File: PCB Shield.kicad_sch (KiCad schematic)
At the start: 49 parts, among them J1 Conn_01x20, J10 Conn_01x04_Socket, J11 Conn_01x04_Socket, J12 TB002-500-02BE, J13 TB002-500-02BE, J14 TB002-500-02BE, J15 TB002-500-02BE, J16 TB002-500-02BE, J17 TB002-500-02BE, J18 TB002-500-02BE, J19 TB002-500-02BE, J2 Conn_01x20, J3 Conn_01x20, J4 Conn_01x20, J5 TB002-500-02BE, J6 Conn_01x08_Socket, J9 Conn_01x04_Socket, Q1 NMOS, U1 74AHCT125S14-13

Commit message: 5:30am progress so far
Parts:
- removed C10, C5, C6, C7, C8, C9: 470uF, Capacitor_SMD:C_1206_3216Metric, symbol Device:C
- removed D1, D2, D3, D4, D5, D6, D7, D8: CMD17-21VGD/TR8, 1A PCB 196:LED0805N_CML, symbol 1A 196 schematics:LED_CMD17-21VGD_TR8
- removed J12, J13, J14, J15, J16, J17, J5: TB002-500-02BE, 1A PCB 196:Conn CUI_TB002-500-02BE, symbol 1A 196 schematics:TB002-500-02BE
- removed R1, R2, R3, R4: 41.2, Resistor_SMD:R_1206_3216Metric_Pad1.30x1.75mm_HandSolder, symbol Device:R
- removed R10, R11, R8, R9: 220, Resistor_SMD:R_1206_3216Metric_Pad1.30x1.75mm_HandSolder, symbol Device:R
- removed VR2: 100K, 1A PCB 196:Pot 3361P-1-104GLF, symbol 1A 196 schematics:Pot 3361P-1-104GLF
- added C10, C4, C5, C6, C7, C9: 470uF, 196_Project_Footprints:CAP_YX_10X12P5_RUB, symbol 196_Project:CAP ALUM 470UF 20% 25V RADIAL TH
- added D1, D2, D3, D4, D5, D6, D7, D8: CMD17-21VGD/TR8, 196_Project_Footprints:LED0805N_CML, symbol 196_Project:LED_CMD17-21VGD_TR8
- added J11, J12, J13, J14, J16, J17: TB002-500-02BE, 196_Project_Footprints:Conn CUI_TB002-500-02BE, symbol 196_Project:TB002-500-02BE
- added J9: OSTT7020150, 196_Project_Footprints:CONN2_OSTT7020150_OST, symbol 196_Project:OSTT7020150
- added R1, R2, R3, R4: 62.6, 196_Project_Footprints:RES 61.2 OHM 1 14W 1206, symbol 196_Project:RES_61.2_OHM_1%_1/4W_1206
- added R6, R7, R8, R9: 220, 196_Project_Footprints:RES 220 OHM 1 1.4W 1206, symbol 196_Project:RES 220 OHM 1% 1/4W 1206
- added U1: ESDA6V1L, 196_Project_Footprints:SOT_DA6V1L_STM-M, symbol 196_Project:ESDA6V1L
- added VR1: 100K, 196_Project_Footprints:Pot 3361P-1-104GLF, symbol 196_Project:Pot 3361P-1-104GLF
- C1: renamed from C11; value 1uF -> C
- C2: renamed from C1; value 0.1uF -> C
- C3: value 1uF -> C
- C8: renamed from C2; value 0.1uF -> C
- R5: value 220 -> R
- renumbered J18 to J10, J19 to J15, J6 to J2, J2 to J4, J4 to J5, J9 to J6, J10 to J7, J11 to J8, U1 to U2, VR3 to VR2
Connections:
- net 5V: now also C10.1, C4.1, C5.1, C6.1, C7.1, C9.1, J11.1, J12.1, J13.1, J14.1, J16.1, J17.1, J9.1, U1.1, U1.2, VR1.1
- net DATA 1Y: now also R7.2
- net DATA 2Y: now also R6.2
- net DATA 3Y: now also R8.2
- net DATA 4Y: now also R9.2
- net GND: now also C10.2, C4.2, C5.2, C6.2, C7.2, C9.2, D2.1, D4.1, D6.1, D8.1, J11.2, J12.2, J13.2, J14.2, J16.2, J17.2, J9.2, U1.3, VR1.3
- net LED split: now also R1.2, R2.2, R3.2, R4.2
- net at J15.2: now also R8.1
- net at Q1.1 (D): now also VR1.2
- net at J10.1: now also R7.1
- net at J10.2: now also R6.1
- net at J15.1: now also R9.1
- new net: D1.1, D2.2
- new net: D5.1, D6.2
- new net: D5.2, R3.1
- new net: D1.2, R1.1
- new net: D3.2, R2.1
- new net: D7.1, D8.2
- new net: D7.2, R4.1
- new net: D3.1, D4.2
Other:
- note added: "Coonnector Guide 1 - High / + 2 - Low / - / GND"
- note added: "Replace passives with my parts"
- note added: "next to Drain"
- note removed: "1. Add switch (30A min) 2. Replace passives with my parts"

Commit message: Finally done?
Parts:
- removed J10, J15: TB002-500-02BE, 1A PCB 196:Conn CUI_TB002-500-02BE, symbol 1A 196 schematics:TB002-500-02BE
- removed LS1: AI-3035-TWT-3V-R, 1A PCB 196:Buzzer XDCR_AI-3035-TWT-3V-R, symbol 1A 196 schematics:AI-3035-TWT-3V-R
- removed U2: 74AHCT125S14-13, 1A PCB 196:74AHCT125S14-13, symbol 1A 196 schematics:74AHCT125S14-13
- removed VR2: 10K, 1A PCB 196:Pot 3361P-1-103GLF, symbol 1A 196 schematics:Pot 3361P-1-103GLF
- added J15, J18: TB002-500-02BE, 196_Project_Footprints:Conn CUI_TB002-500-02BE, symbol 196_Project:TB002-500-02BE
- added LS1: Buzzer AI-3035-TWT-3V-R, 196_Project_Footprints:Buzzer XDCR_AI-3035-TWT-3V-R, symbol 196_Project:Buzzer AI-3035-TWT-3V-R
- added U2: 74AHCT125S14-13, 196_Project_Footprints:74AHCT125S14-13, symbol 196_Project:74AHCT125S14-13
- added VR2: 10K, 196_Project_Footprints:Pot 3361P-1-103GLF, symbol 196_Project:Pot 3361P-1-103GLF
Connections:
- net 3V3: now also VR2.1
- net 5V: now also U2.14 (VCC)
- net A1 / IO3: now also U2.2 (1A)
- net ADC1 / IO1: now also VR2.2
- net DATA 1Y: now also U2.3 (1Y)
- net DATA 2Y: now also U2.6 (2Y)
- net DATA 3Y: now also U2.8 (3Y)
- net DATA 4Y: now also U2.11 (4Y)
- net EN1 / IO2: now also U2.1 (*1OE)
- net GND: now also LS1.N, U2.7 (GND), VR2.3
- net IO37: now also U2.4 (*2OE)
- net IO38: now also U2.5 (2A)
- net IO41: now also U2.9 (3A)
- net IO42: now also U2.10 (*3OE)
- net IO43: now also U2.12 (4A)
- net IO44: now also U2.13 (*4OE)
- net PWM / IO16: now also LS1.P
- net at R9.1: now also J18.1
- net at R7.1: now also J15.1
- net at R6.1: now also J15.2
- net at R8.1: now also J18.2

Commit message: Hopefully this works
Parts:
- removed U1: ESDA6V1L, 196_Project_Footprints:SOT_DA6V1L_STM-M, symbol 196_Project:ESDA6V1L
- added U3: ESDA6V1L, 196_Project_Footprints:SOT_DA6V1L_STM-M, symbol 196_Project:ESDA6V1L
- J9: MANUFACTURER CUI -> (none); STANDARD Manufacturer Recommendations -> (none)
- renumbered J15 to J10, J18 to J15
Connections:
- net 5V: now also U3.1, U3.2
- net GND: now also U3.3

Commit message: 4/27 work today
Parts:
- removed C1, C3: C, Capacitor_SMD:C_1206_3216Metric, symbol Device:C
- removed C2, C8: C, symbol Device:C
- removed C4: 470uF, 196_Project_Footprints:CAP_YX_10X12P5_RUB, symbol 196_Project:CAP ALUM 470UF 20% 25V RADIAL TH
- removed J11: TB002-500-02BE, 196_Project_Footprints:Conn CUI_TB002-500-02BE, symbol 196_Project:TB002-500-02BE
- removed R5: R, Resistor_SMD:R_1206_3216Metric_Pad1.30x1.75mm_HandSolder, symbol Device:R
- removed VR1: 100K, 196_Project_Footprints:Pot 3361P-1-104GLF, symbol 196_Project:Pot 3361P-1-104GLF
- added C1, C3: 0.1uF, 196_Project_Footprints:CAP CER 0.1UF 50V X7R 1206, symbol 196_Project:CAP_CER_0.1UF_50V_X7R_1206
- added C11: 470uF, 196_Project_Footprints:CAP_YX_10X12P5_RUB, symbol 196_Project:CAP ALUM 470UF 20% 25V RADIAL TH
- added C2: 1uF, 196_Project_Footprints:CAP SMD 1206 X7R 1UF 10 25V, symbol 196_Project:CAP_SMD_1206_X7R_1UF_25V
- added J18: TB002-500-02BE, 196_Project_Footprints:Conn CUI_TB002-500-02BE, symbol 196_Project:TB002-500-02BE
- added Q2: NMOS, symbol Simulation_SPICE:NMOS
- added R11, R12, R13: 220, 196_Project_Footprints:RES 220 OHM 1 1.4W 1206, symbol 196_Project:RES 220 OHM 1% 1/4W 1206
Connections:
- net 3V3: no longer J1.19 (Pin_19), J2.8 (Pin_8), J3.19 (Pin_19)
- net GATE / IO45: now also Q2.2 (G), R11.1; no longer J4.2 (Pin_2), Q1.2 (G)
- net GND: now also J1.GND (Pin_20), J3.GND (Pin_20), Q1.3 (S), C1.1, C11.2, C2.1, C3.1, J18.2, R11.2; no longer D2.1, D4.1, D6.1, D8.1, J1.20 (Pin_20), J3.20 (Pin_20), J4.20 (Pin_20)
- net IO37: no longer J4.10 (Pin_10)
- net IO38: no longer J4.9 (Pin_9)
- net IO41: no longer J4.6 (Pin_6)
- net IO42: no longer J4.5 (Pin_5)
- net IO43: no longer J4.4 (Pin_4)
- net IO44: no longer J4.3 (Pin_3)
- net LED split: now also D2.1, D4.1, D6.1, D8.1, Q1.1 (D); no longer Q1.3 (S), R1.2, R2.2, R3.2, R4.2
- net PWM / IO16: no longer J4.1 (Pin_1)
- net at J5.11 (Pin_11): no longer J4.11 (Pin_11)
- net at J5.12 (Pin_12): no longer J4.12 (Pin_12)
- net at J5.13 (Pin_13): no longer J4.13 (Pin_13)
- net at J5.14 (Pin_14): no longer J4.14 (Pin_14)
- net at J5.15 (Pin_15): no longer J4.15 (Pin_15)
- net at J5.16 (Pin_16): no longer J4.16 (Pin_16)
- net at J5.17 (Pin_17): no longer J4.17 (Pin_17)
- net at J5.18 (Pin_18): no longer J4.18 (Pin_18)
- net at J5.7 (Pin_7): no longer J4.7 (Pin_7)
- net at J5.8 (Pin_8): no longer J4.8 (Pin_8)
- net 5V renamed +5V
- net +5V: now also R1.2, R2.2, R3.2, R4.2, C1.2, C11.1, C2.2, C3.2, J18.1, Q2.1 (D); no longer J4.19 (Pin_19)
- new net +3V3: J1.3V3 (Pin_19), J2.8 (Pin_8), J3.3V3 (Pin_19)
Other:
- note added: "5V/(4*5ma) = ? Ohms"
- note added: "Expected 20mA"
- note added: "I2C pull ups"
- note added: "Low end NMOS"
- note added: "Total current: ~18.5 A Power: 92W --> 100W power supply ^ worst case, max brightness, RBG fully on unicolor --> 6A 50% brightness cap --> I/2 As long as we never go full white, 10A power supply is okay"
- note added: "connect to NMOS drain"
- note removed: "5V/(4*20ma) = 62.2 Ohms"
- note removed: "Expected 80mA"
- note removed: "Replace passives with my parts"
- note removed: "Total current: ~18.5 A Power: 92W --> 100W power supply ^ worst case, max brightness, RBG fully on unicolor --> 6A 50% brightness cap --> I/2"
- note removed: "next to Drain"
- note removed: "potentiometer as brightness control and extra protection"
- moved on the sheet: C10, C5, C7, D1, D2, D3, D4, D5, D6, D7, D8, J10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

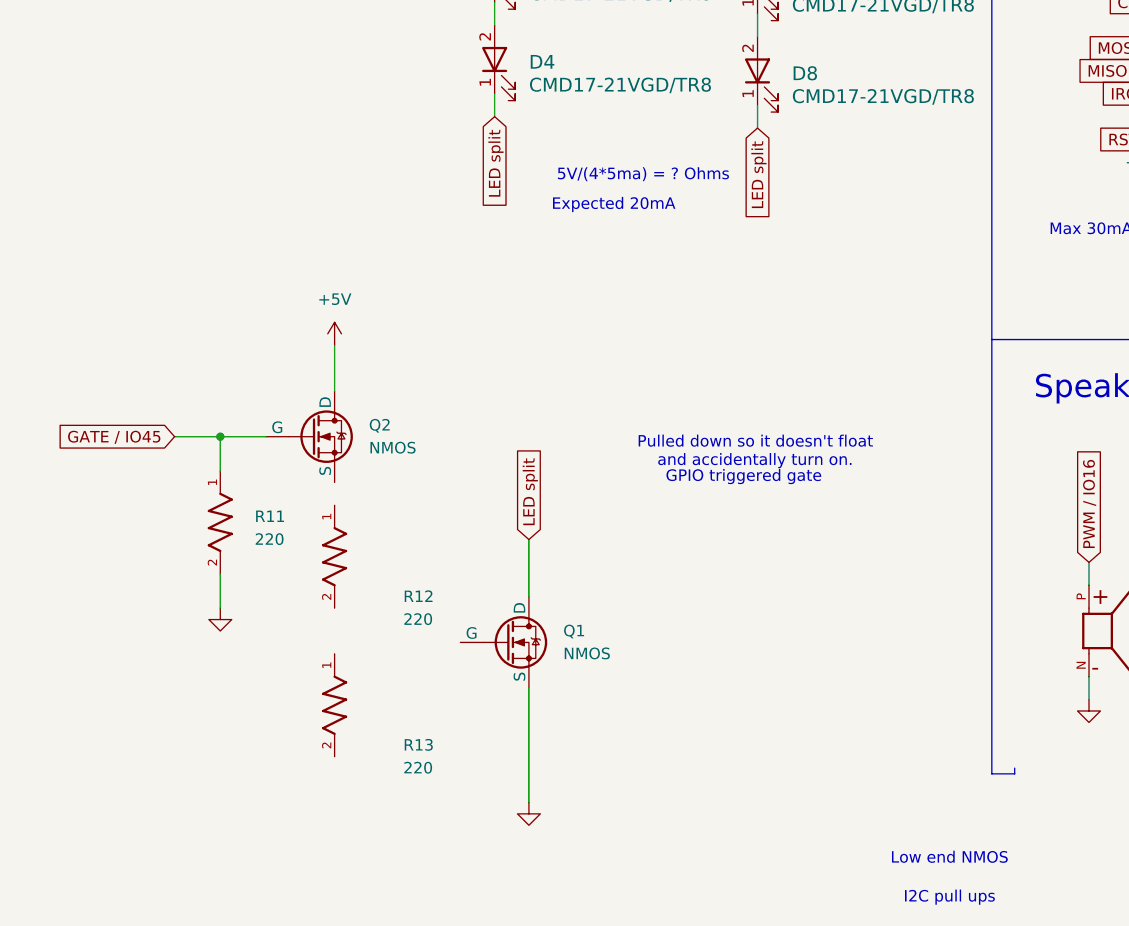
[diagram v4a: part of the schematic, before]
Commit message: gave all footprints proper names and descriptions
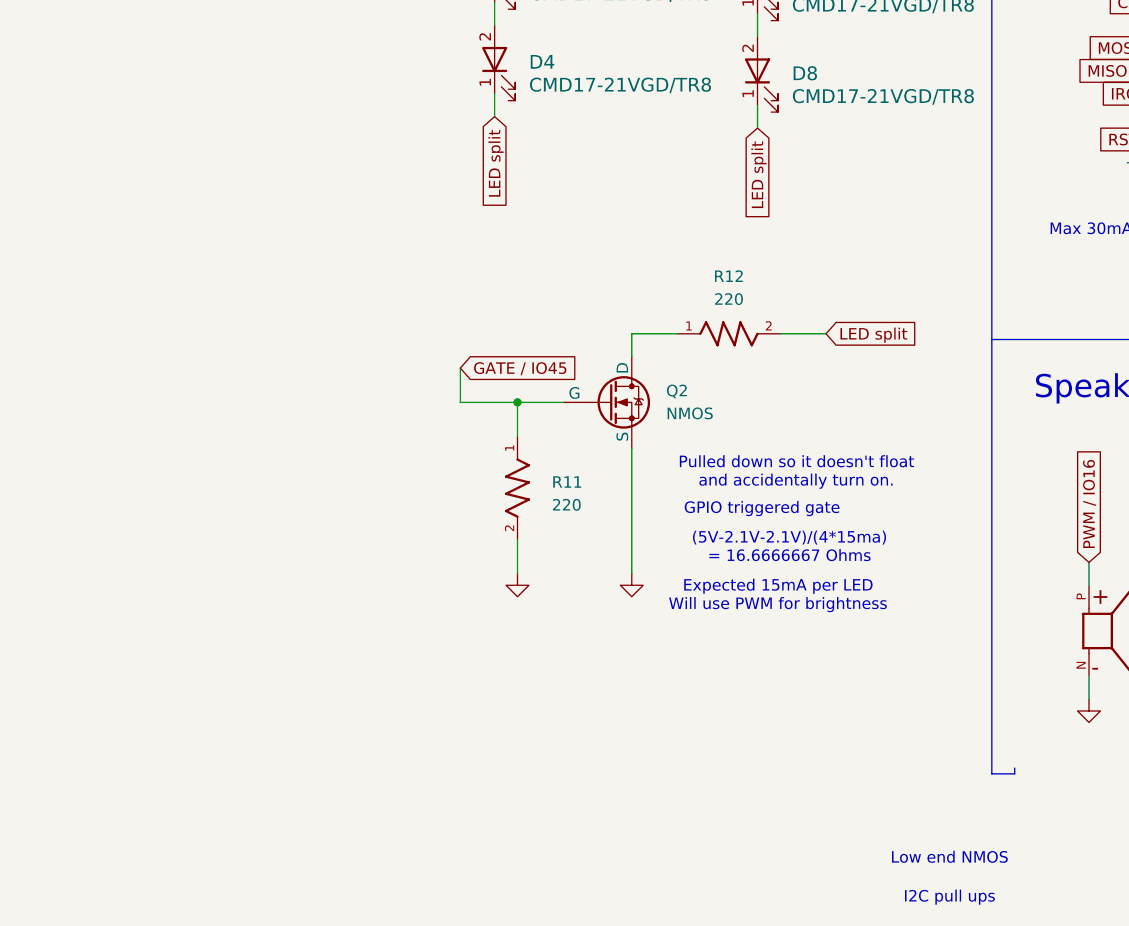
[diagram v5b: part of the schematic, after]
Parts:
- removed Q1: NMOS, symbol Simulation_SPICE:NMOS
- removed R13: 220, 196_Project_Footprints:RES 220 OHM 1 1.4W 1206, symbol 196_Project:RES 220 OHM 1% 1/4W 1206
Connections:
- net +5V: no longer Q2.1 (D)
- net GND: now also Q2.3 (S)
- net LED split: now also R12.2
- net at R12.1: now also Q2.1 (D)
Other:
- note added: "(5V-2.1V-2.1V)/(4*15ma) = 16.6666667 Ohms"
- note added: "Expected 15mA per LED Will use PWM for brightness"
- note removed: "5V/(4*5ma) = ? Ohms"
- note removed: "Expected 20mA"
- moved on the sheet: Q2, R11

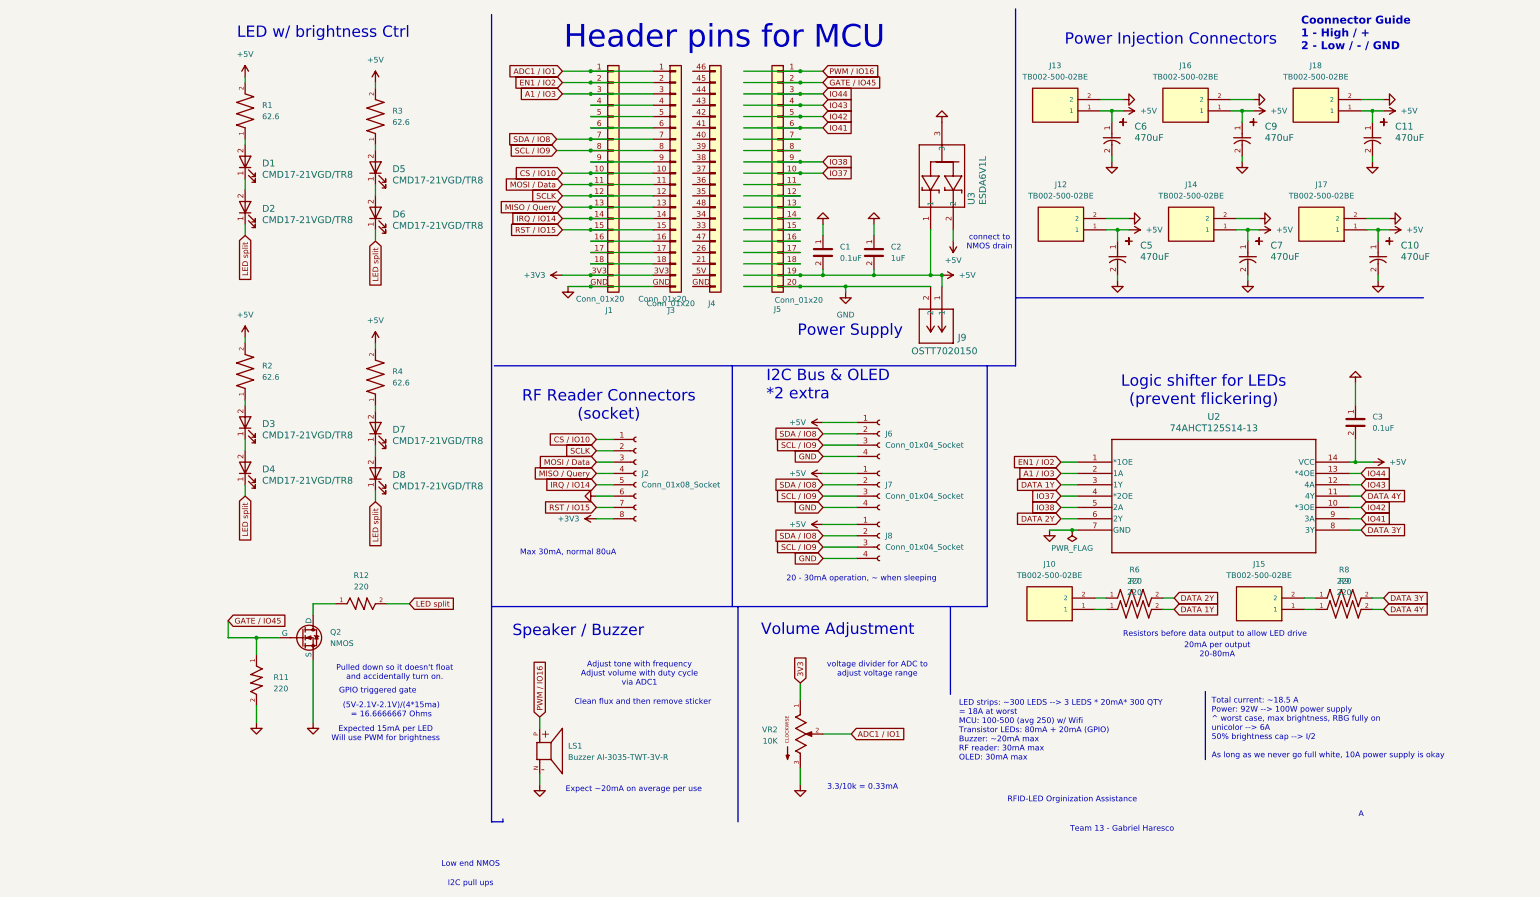
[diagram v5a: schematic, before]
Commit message: added transistor to libraries
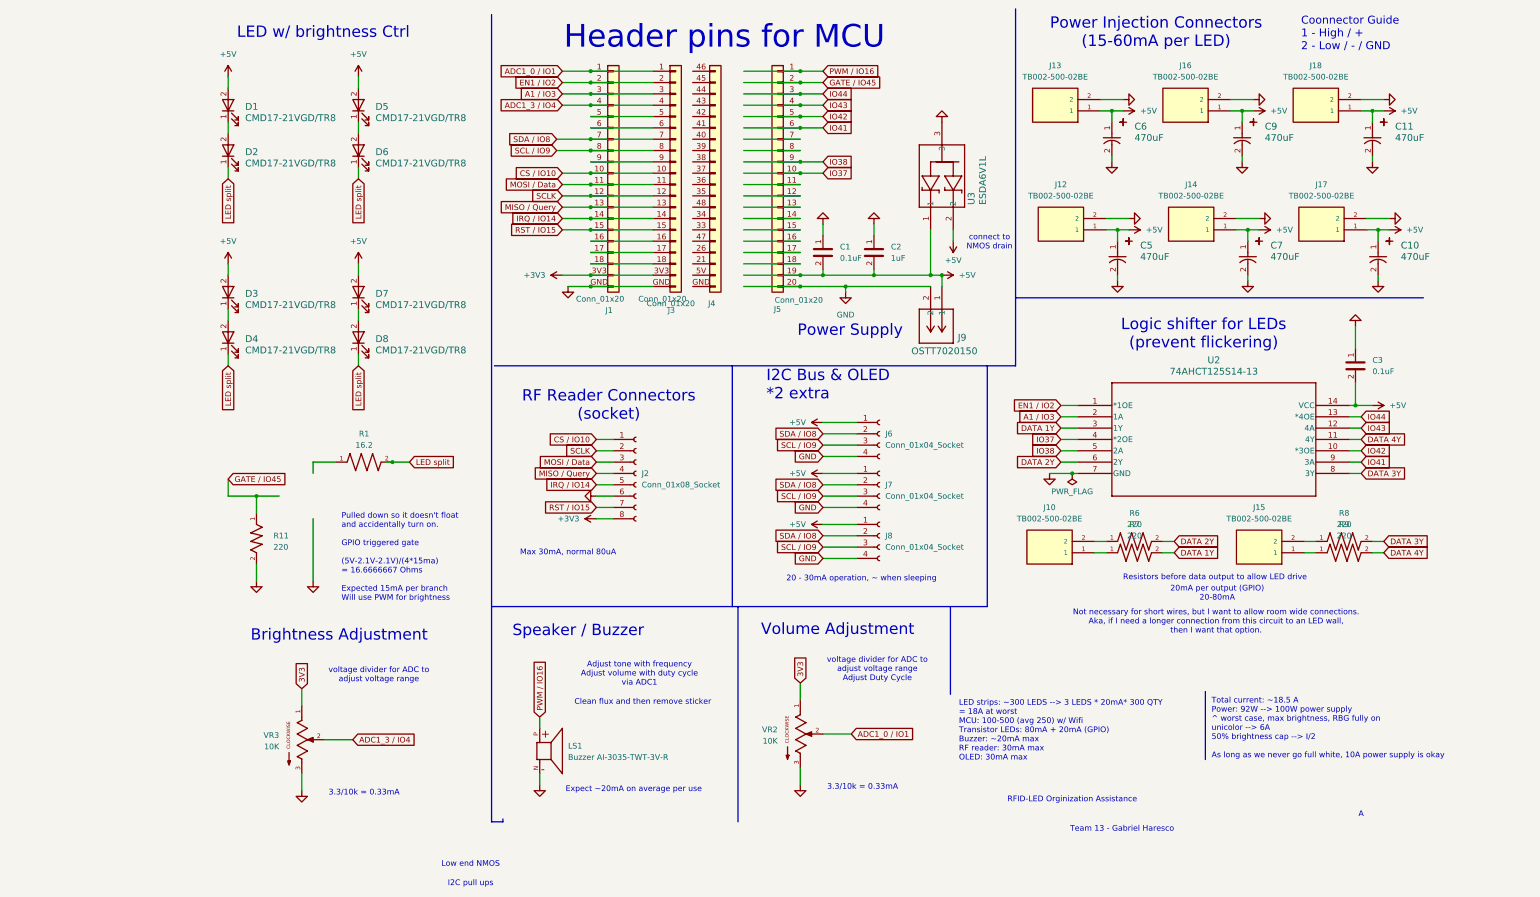
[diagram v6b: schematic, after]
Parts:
- removed Q2: NMOS, symbol Simulation_SPICE:NMOS
- removed R1, R2, R3, R4: 62.6, 196_Project_Footprints:RES 61.2 OHM 1 14W 1206, symbol 196_Project:RES_61.2_OHM_1%_1/4W_1206
- removed R12: 220, 196_Project_Footprints:RES 220 OHM 1 1.4W 1206, symbol 196_Project:RES 220 OHM 1% 1/4W 1206
- added R1: 16.2, 196_Project_Footprints:CRCW120616R2FKEA, symbol 196_Project:CRCW120616R2FKEA
- added VR3: 10K, 196_Project_Footprints:Pot 3361P-1-103GLF, symbol 196_Project:Pot 3361P-1-103GLF
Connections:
- net +5V: now also D1.2, D3.2, D5.2, D7.2
- net 3V3: now also VR3.1
- net GND: now also VR3.3
- net LED split: now also R1.2
- net ADC1_3 / IO4: now reaches J1.4 (Pin_4), J3.4 (Pin_4)
- net ADC1_3 / IO4: now also VR3.2
- net ADC1 / IO1 renamed ADC1_0 / IO1
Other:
- note added: "20mA per output (GPIO) 20-80mA"
- note added: "Brightness Adjustment"
- note added: "Not necessary for short wires, but I want to allow room wide connections. Aka, if I need a longer connection from this circuit to an LED wall, then I want that option."
- note added: "Power Injection Connectors (15-60mA per LED)"
- note added: "Pulled down so it doesn't float and accidentally turn on. GPIO triggered gate (5V-2.1V-2.1V)/(4*15ma) = 16.6666667 Ohms Expected 15mA per branch Will use PWM for brightness"
- note added: "voltage divider for ADC to adjust voltage range Adjust Duty Cycle"
- note removed: "(5V-2.1V-2.1V)/(4*15ma) = 16.6666667 Ohms"
- note removed: "20mA per output 20-80mA"
- note removed: "Expected 15mA per LED Will use PWM for brightness"
- note removed: "GPIO triggered gate"
- note removed: "Power Injection Connectors"
- note removed: "Pulled down so it doesn't float and accidentally turn on."
- moved on the sheet: C3, D1, D2, D3, D4, D5, D6, D7, D8, J10, J15, R11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

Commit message: added switch
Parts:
- added Q1: IRLML2502TRPBF, 196_Project_Footprints:SOT95P237X112-3N-2-V, symbol 196_Project:IRLML2502TRPBF
- added SW1: C1353VQNAA, 196_Project_Footprints:C1353VQNAA, symbol 196_Project:C1353VQNAA
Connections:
- net +5V: now also SW1.2; no longer C1.2, C2.2, J5.19 (Pin_19)
- net GATE / IO45: now also J4.45 (Pin_2), J5.45 (Pin_2), Q1.2 (G); no longer J5.2 (Pin_2)
- net GND: now also C1.2, C2.2, J4.GND (Pin_20), J5.GND (Pin_20), Q1.3 (S); no longer C1.1, C2.1, J5.20 (Pin_20)
- net IO37: now also J4.37 (Pin_10), J5.37 (Pin_10); no longer J5.10 (Pin_10)
- net IO38: now also J4.38 (Pin_9), J5.38 (Pin_9); no longer J5.9 (Pin_9)
- net IO41: now also J4.41 (42), J5.41 (42); no longer J5.6 (Pin_6)
- net IO42: now also J4.42 (Pin_5), J5.42 (Pin_5); no longer J5.5 (Pin_5)
- net IO43: now also J4.43 (Pin_4), J5.43 (Pin_4); no longer J5.4 (Pin_4)
- net IO44: now also J4.44 (Pin_3), J5.44 (Pin_3); no longer J5.3 (Pin_3)
- net PWM / IO16: now also J4.46 (Pin_1), J5.46 (Pin_1); no longer J5.1 (Pin_1)
- net at R1.1: now also Q1.1 (D)
- net at J4.21 (Pin_18): now also J5.21 (Pin_18)
- net at J4.26 (Pin_17): now also J5.26 (Pin_17)
- net at J4.33 (Pin_15): now also J5.33 (Pin_15)
- net at J4.34 (Pin_14): now also J5.34 (Pin_14)
- net at J4.35 (Pin_12): now also J5.35 (Pin_12)
- net at J4.36 (Pin_11): now also J5.36 (Pin_11)
- net at J4.39 (Pin_8): now also J5.39 (Pin_8)
- net at J4.40 (Pin_7): now also J5.40 (Pin_7)
- net at J4.47 (Pin_16): now also J5.47 (Pin_16)
- net at J4.48 (Pin_13): now also J5.48 (Pin_13)
- net at J4.5V (Pin_19): now also C1.1, C2.1, J5.5V (Pin_19), SW1.1
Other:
- note removed: "I2C pull ups"
- note removed: "Low end NMOS"
- moved on the sheet: J4, J9, U3
